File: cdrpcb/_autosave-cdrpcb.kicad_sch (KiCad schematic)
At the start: 41 parts, among them J1 Conn_02x04_Odd_Even, J2 Conn_01x03, J3 Conn_01x03, J4 Conn_01x03, J5 Conn_01x03, J7 Conn_01x06, J8 Conn_01x04, J9 Conn_01x03, SW1 Conn_01x02_Pin, SW2 Conn_01x02_Pin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

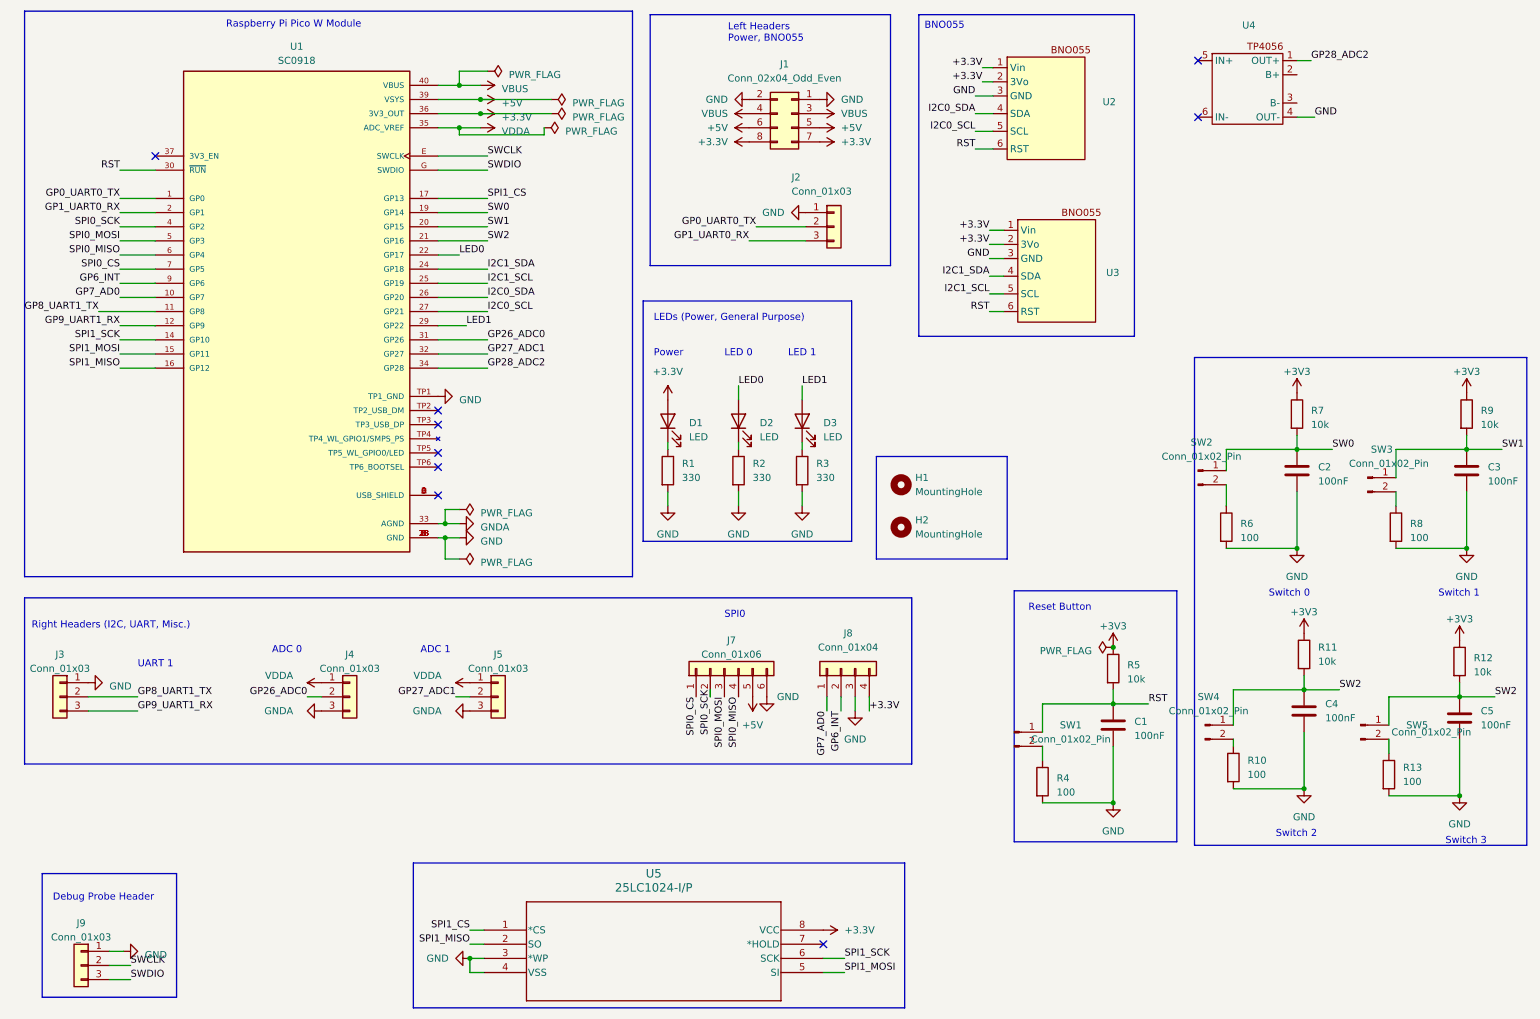
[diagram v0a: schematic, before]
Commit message: PCB iteration with download, drill and appropriately named schematic
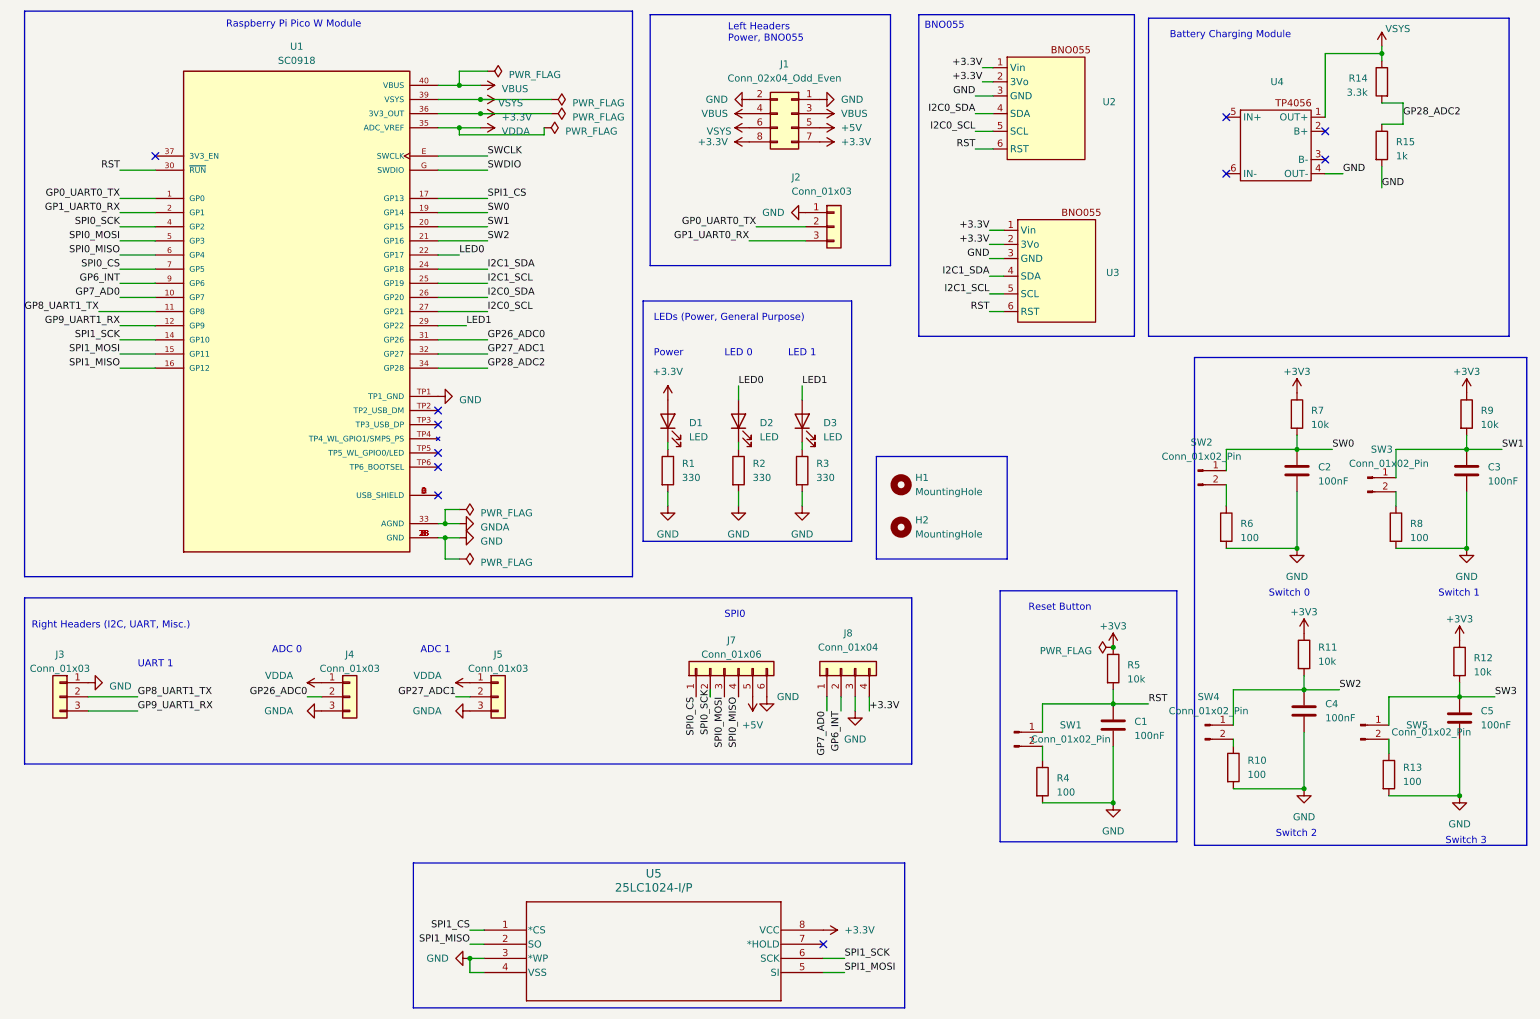
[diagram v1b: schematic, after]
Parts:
- removed J9: Conn_01x03, Connector_PinHeader_2.54mm:PinHeader_1x03_P2.54mm_Vertical, symbol Connector_Generic:Conn_01x03
- added R14: 3.3k, Resistor_THT:R_Axial_DIN0204_L3.6mm_D1.6mm_P1.90mm_Vertical, symbol Device:R
- added R15: 1k, Resistor_THT:R_Axial_DIN0204_L3.6mm_D1.6mm_P1.90mm_Vertical, symbol Device:R
- J8: footprint (none) -> Connector_PinHeader_2.54mm:PinHeader_1x04_P2.54mm_Vertical
- SW1, SW2, SW3, SW4, SW5: footprint (none) -> Connector_PinHeader_2.54mm:PinHeader_1x02_P2.54mm_Vertical
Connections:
- net +5V: now also U4.1 (OUT+), R14.1
- net GND: now also R15.2
- net GP28_ADC2: now also R14.2, R15.1; no longer U4.1 (OUT+)
- net SW2: no longer C5.1, R12.2, SW5.1 (Pin_1)
- new net SW3: C5.1, R12.2, SW5.1 (Pin_1)
- no-connect marks 9 -> 11
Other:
- note added: "Battery Charging Module"
- note removed: "Debug Probe Header"
- company: (none) -> SDP 2024 Team 16
- title: (none) -> CDR PCB - InSight
- moved on the sheet: U4
